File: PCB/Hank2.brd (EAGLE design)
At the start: 256.5 x 129.5 mm, 112 parts, among them IC3 ATMEGA328-20P, T1 2n2222, T2 2n2222, T3 2n2222, T4 2n2222, T5 2n2222, T6 2n2222, T7 2n2222, T8 2n2222, X1 Sockets 1, X2 Sockets 2

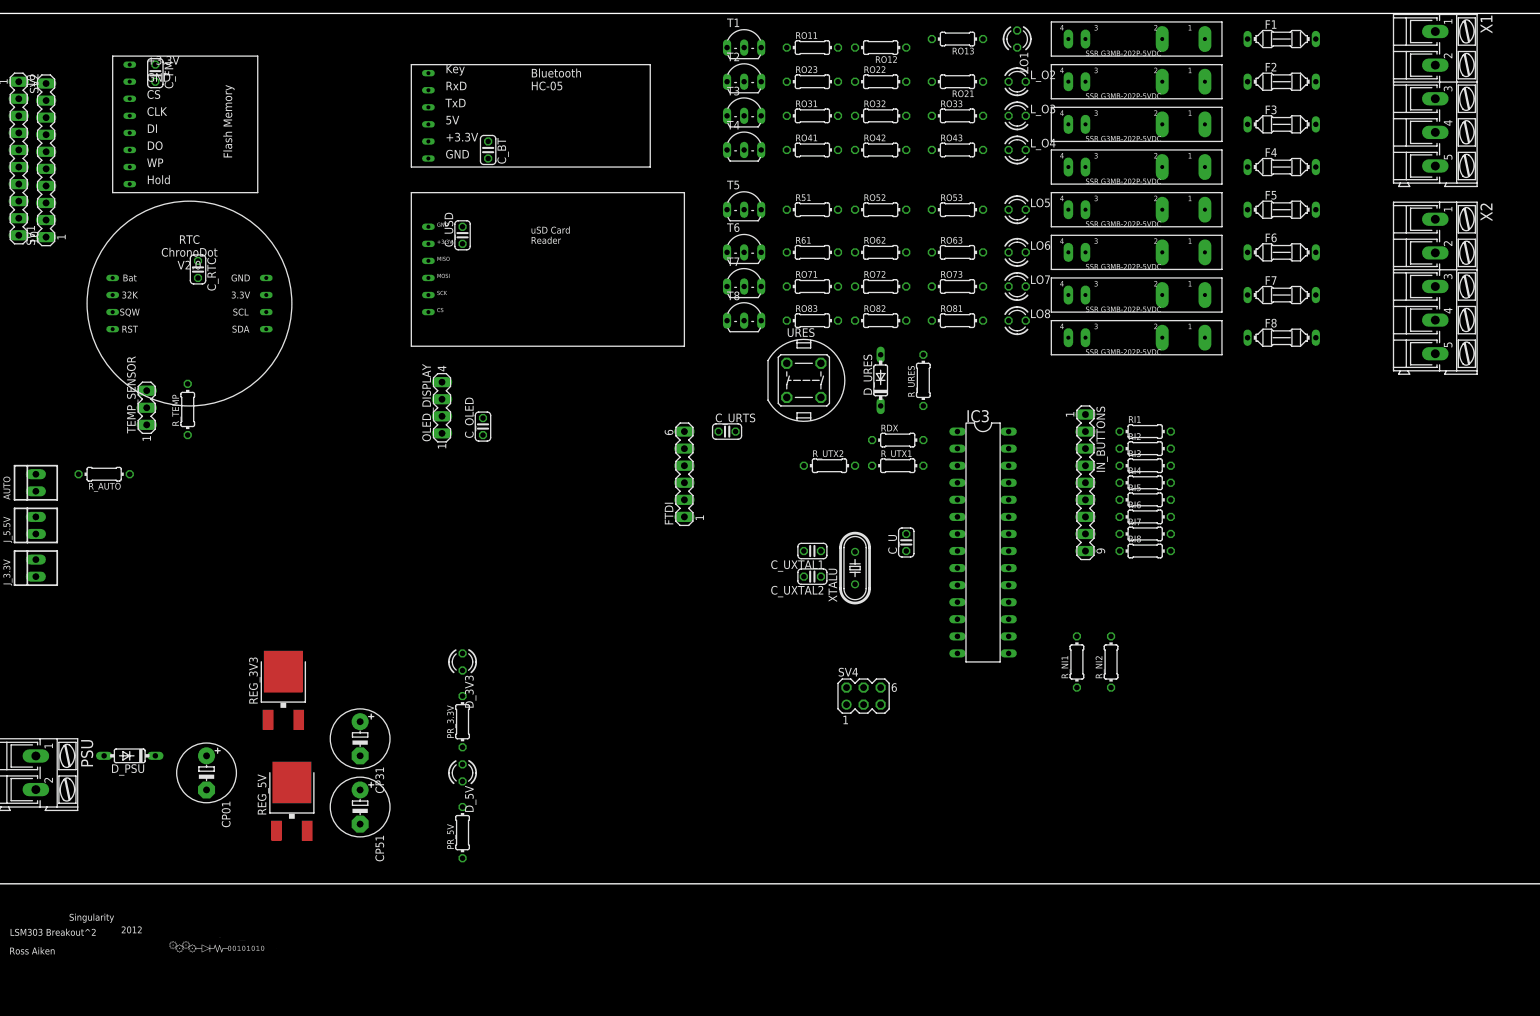
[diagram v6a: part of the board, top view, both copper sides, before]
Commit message: Changed the VRegs and Added a crowbar circuit to handle overvoltage conditions
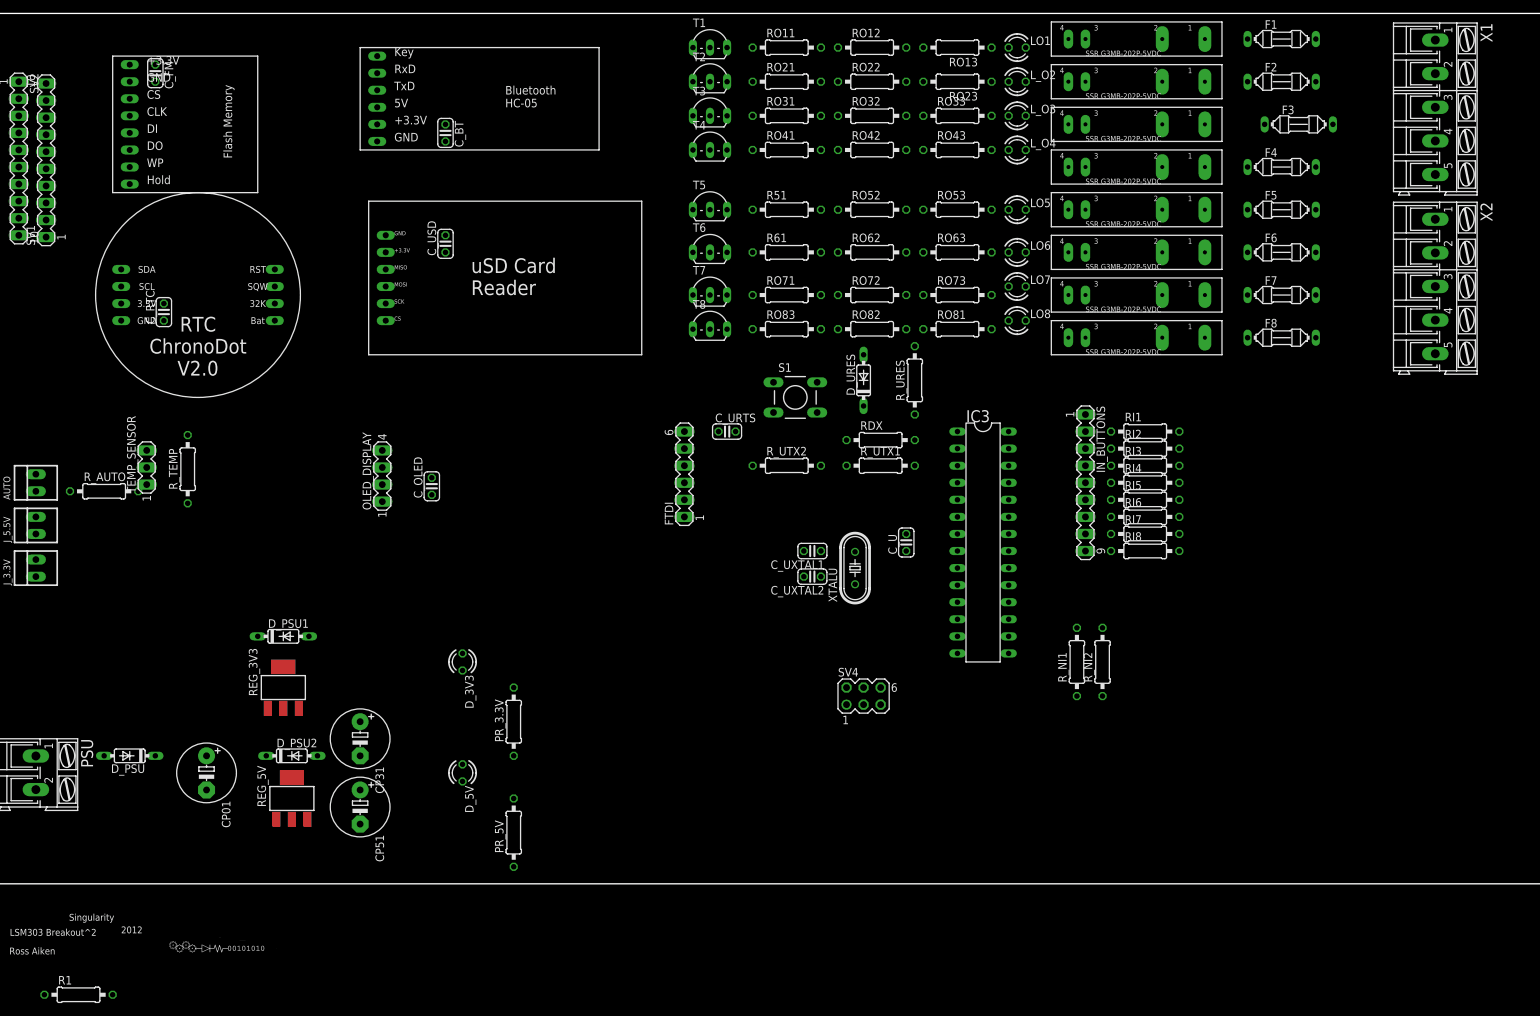
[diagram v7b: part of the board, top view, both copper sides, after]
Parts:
- removed URES: DTE6, switch-misc:DTE6
- added D_PSU1, D_PSU2: 1N4148DO35-7, diode:DO35-7
- added R1: (no value), rcl:0207/10
- added S1: DTS-6, switch-tact:DTS-6
- PR_3.3V, PR_5V, R51, R61, RDX, RI1, RI2, RI3, RI4, RI5, RI6, RI7, RI8, RO11, RO12, RO13, RO21, RO22, RO23, RO31, RO32, RO33, RO41, RO42, RO43, RO52, RO53, RO62, RO63, RO71, RO72, RO73, RO81, RO82, RO83, R_AUTO, R_NI1, R_NI2, R_TEMP, R_URES, R_UTX1, R_UTX2: device rcl:0204/7 -> rcl:0207/10
- REG_3V3: value LP2950CDT-3.3 -> AMS1117; device v-reg:DPACK -> AMS117:SOT223
- REG_5V: value LP2950CDT-5.0 -> AMS1117; device v-reg:DPACK -> AMS117:SOT223
- moved RO21 25.4 mm to (119.4, 119.4), turned to 0 degrees
- moved RO23 21.6 mm to (144.8, 119.4), turned to 180 degrees
- moved OLED_DISPLAY 13.5 mm to (59.2, 60.7)
- moved C_OLED 11.7 mm to (66.5, 59.2)
- moved R_TEMP 8.89 mm to (30.2, 61.7)
- moved TEMP_SENSOR 8.89 mm to (24.1, 62.0)
- moved C_RTC 8.13 mm to (26.7, 85.1), turned to 90 degrees
- moved PR_3.3V 7.62 mm to (78.7, 24.1)
- moved PR_5V 7.62 mm to (78.7, 7.62)
- moved C_BT 6.84 mm to (68.6, 111.8)
- moved U$7 6.48 mm to (77.5, 90.2)
- moved R_UTX2 6.35 mm to (119.4, 62.2)
- moved T7 5.24 mm to (108.0, 87.6)
- moved U$4 5.24 mm to (73.7, 116.8)
- moved T8 5.24 mm to (108.0, 82.5)
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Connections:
- net +3V3: now also D_PSU2.A, REG_3V3.2, REG_3V3.TAB; no longer REG_3V3.3
- net +5V: now also D_PSU1.A, REG_5V.2, REG_5V.TAB; no longer REG_5V.3
- net CP12: now also D_PSU1.C, D_PSU2.C, REG_3V3.3, REG_5V.3; no longer REG_3V3.1, REG_5V.1
- net GND: now also REG_3V3.1, REG_5V.1, S1.1, S1.2; no longer REG_3V3.4, REG_5V.4, URES.3, URES.4
- net L1-1: now also SSR1.2; no longer SSR1.1
- net N$3: now also SSR1.1; no longer SSR1.2
- net U_RESET: now also S1.3, S1.4; no longer URES.1, URES.2

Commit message: Trying to set up the positions of the components in the PCB
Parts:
- removed R1: (no value), rcl:0207/10
- removed SV1, SV2: (no value), con-lstb:MA10-1
- added SV3: (no value), con-lstb:MA10-2
- PSU: device con-ptr500:AK300/2 -> con-ptr500:AK500/2
- X1, X2: device con-ptr500:AK300/5 -> con-ptr500:AK500/5
- moved R_UTX1 114.6 mm to (19.1, 69.8)
- moved C_USD 109.1 mm to (-30.5, 49.5)
- moved U$4 101.4 mm to (47.0, 19.1), turned to 90 degrees
- moved R_UTX2 100.4 mm to (19.1, 66.0)
- moved RDX 100.4 mm to (33.0, 63.5), turned to 90 degrees
- moved R_URES 100.0 mm to (48.3, 31.8)
- moved F8 99.8 mm to (133.3, 1.27)
- moved C_URTS 98.6 mm to (33.0, 6.35), turned to 90 degrees
- moved D_URES 98.3 mm to (43.2, 30.5)
- moved F7 95.8 mm to (133.3, 12.7)
- moved RI1 95.7 mm to (77.5, 76.2)
- moved RI2 95.7 mm to (77.5, 73.7)
- moved RI3 95.7 mm to (77.5, 71.1)
- moved RI4 95.7 mm to (77.5, 68.6)
- moved RI5 95.7 mm to (77.5, 66.0)
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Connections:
- removed net MOUT2: F2.1, SSR2.2
- removed net MOUT3: F3.1, SSR3.2
- removed net MOUT4: F4.1, SSR4.2
- removed net MOUT5: F5.1, SSR5.2
- removed net MOUT6: F6.1, SSR6.2
- removed net MOUT7: F7.1, SSR7.2
- removed net MOUT8: F8.1, SSR8.2
- new net N$10: F5.1, SSR5.1
- new net N$13: F6.1, SSR6.1
- new net N$14: F2.1, SSR2.1
- new net N$15: F3.1, SSR3.1
- new net N$19: F7.1, SSR7.1
- new net N$24: F4.1, SSR4.1
- new net N$28: F8.1, SSR8.1
- net AUTO_MANUAL: now also SV3.20; no longer SV2.10
- net BT_RX: now also SV3.7; no longer SV1.4
- net BT_TX: now also SV3.9; no longer SV1.5
- net FLASH_CLK: now also SV3.4; no longer SV2.2
- net FLASH_CS: now also SV3.2; no longer SV2.1
- net FLASH_DI: now also SV3.6; no longer SV2.3
- net FLASH_DO: now also SV3.8; no longer SV2.4
- net GND: now also SV3.5; no longer SV1.3
- net L1-1: now also SSR2.2, SSR3.2, SSR4.2; no longer SSR2.1, SSR3.1, SSR4.1
- net L1-2: now also SSR5.2, SSR6.2, SSR7.2, SSR8.2; no longer SSR5.1, SSR6.1, SSR7.1, SSR8.1
- net MISO: now also SV3.10; no longer SV2.5
- net MOSI: now also SV3.12; no longer SV2.6
- net N$1: now also SV3.1; no longer SV1.1
- net N$2: now also SV3.3; no longer SV1.2
- net NEW_IN: now also SV3.11; no longer SV1.6
- net SCK: now also SV3.14; no longer SV2.7
- net SCL: now also SV3.19; no longer SV1.10
- net SDA: now also SV3.17; no longer SV1.9
- net SD_CS: now also SV3.16; no longer SV2.8
- net TEMP_SEN: now also SV3.18; no longer SV2.9
- net U_RX: now also SV3.13; no longer SV1.7
- net U_TX_3: now also SV3.15; no longer SV1.8
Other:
- board size 256.5 x 129.5 mm -> 149.9 x 100.3 mm
